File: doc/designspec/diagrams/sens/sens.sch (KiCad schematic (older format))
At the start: 16 parts

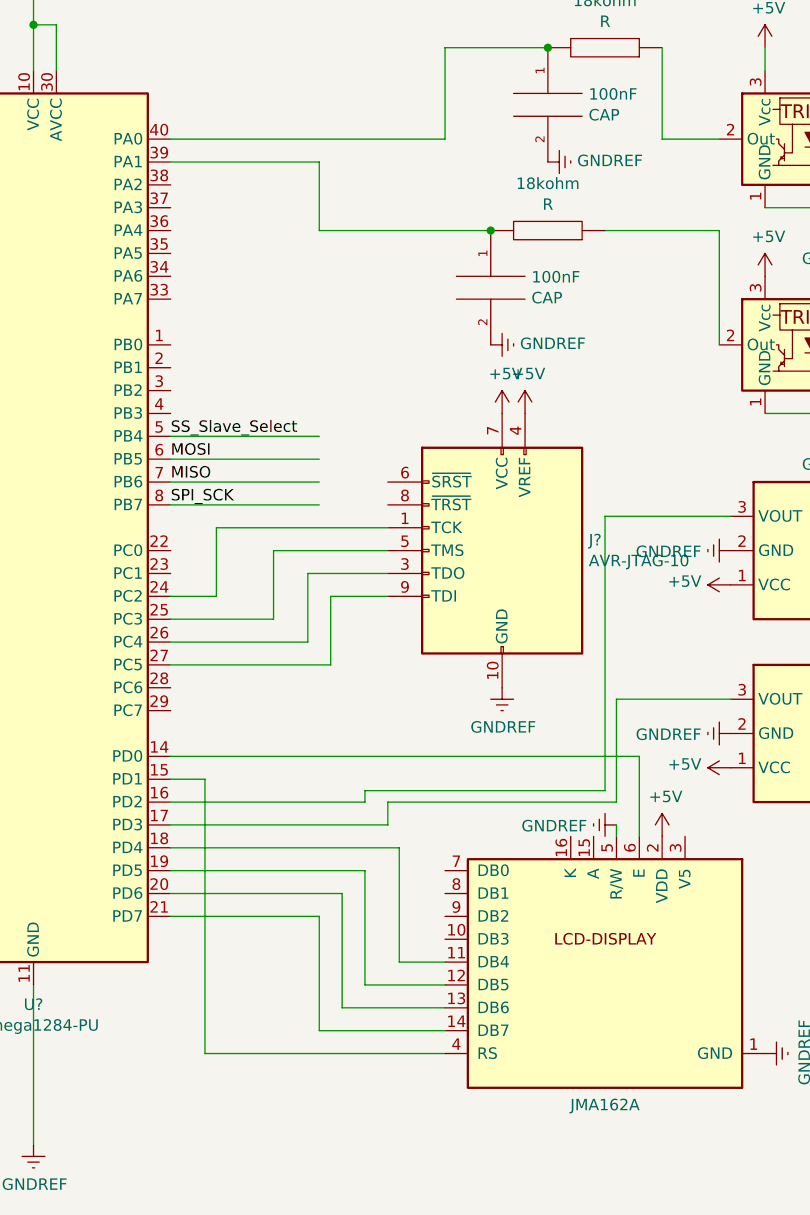
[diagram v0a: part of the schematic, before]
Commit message: update sens module schematic
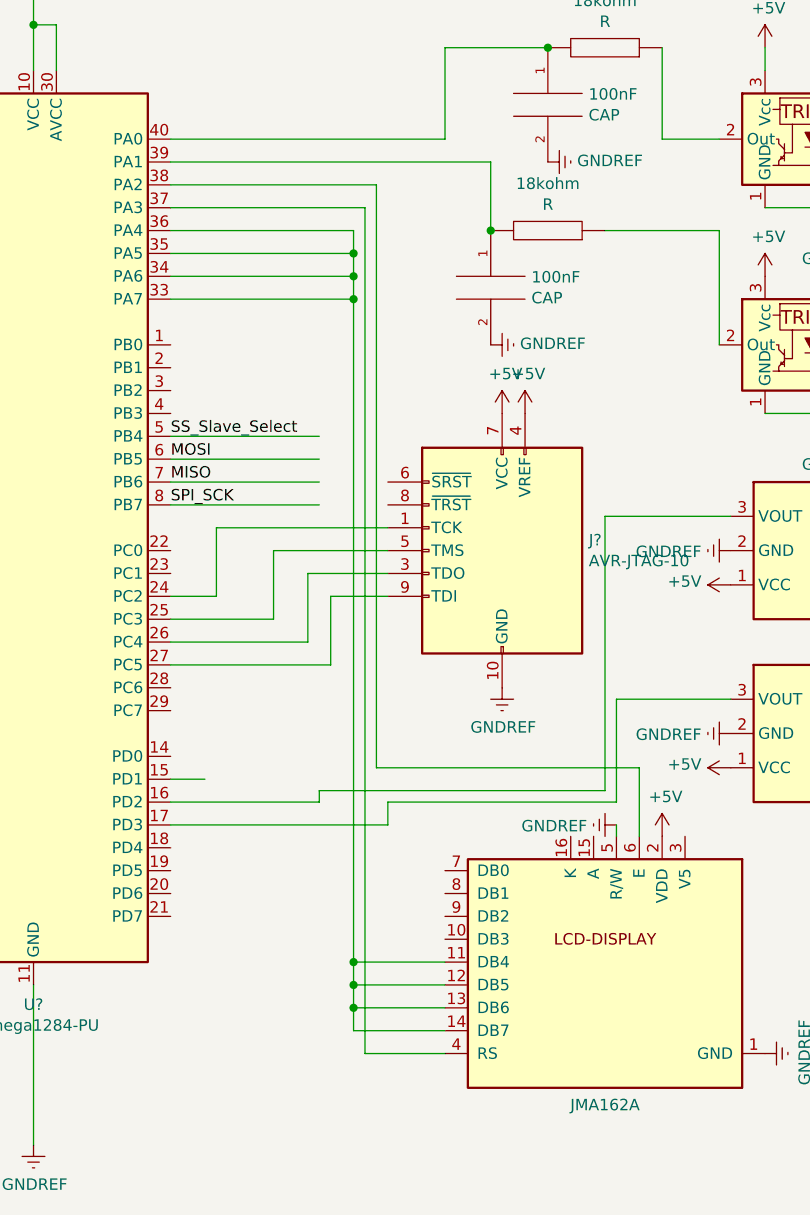
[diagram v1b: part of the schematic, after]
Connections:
- wire segments 74 -> 79

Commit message: Revert "update sens module schematic"
This reverts commit 18ae42b13ac670fb9527cdf2e035fc7bce516c1b.
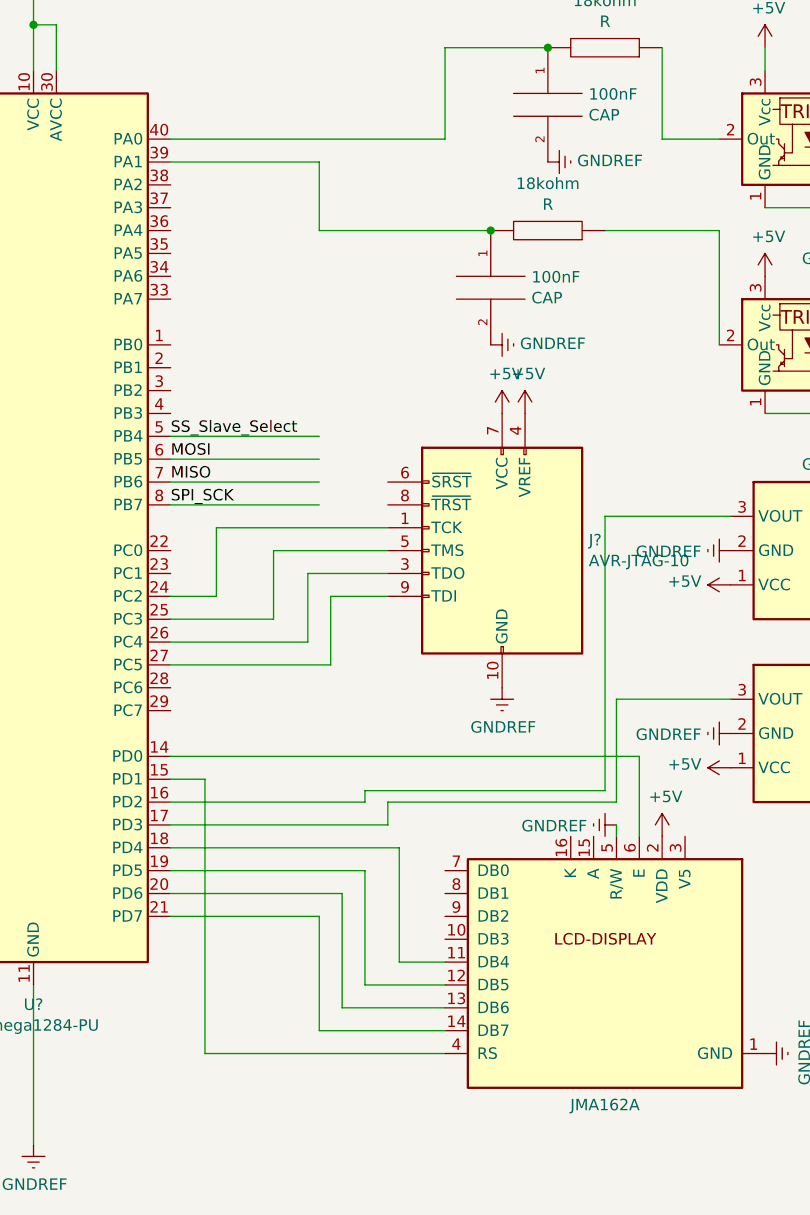
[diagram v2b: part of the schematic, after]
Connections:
- wire segments 79 -> 74
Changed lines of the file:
@@
 Wire Wire Line
 	3700 5150 3700 5850
+Wire Wire Line
+	6900 1050 6900 1150
 $Comp
 L sens-rescue:IQEXO-3-exo3 KRISTALLOSCILLATOR
@@
 	1    0    0    -1
 $EndComp
+$Comp
+L power:GNDREF #PWR?
+U 1 1 5BDF1A61
+P 6900 5450
+F 0 "#PWR?" H 6900 5200 50  0001 C CNN
+F 1 "GNDREF" H 6905 5277 50  0000 C CNN
+F 2 "" H 6900 5450 50  0001 C CNN
+F 3 "" H 6900 5450 50  0001 C CNN
+	1    6900 5450
+	0    -1   -1   0
+$EndComp
 Text Label 4300 2750 0    50   ~ 0
 SS_Slave_Select
@@
 $EndComp
 $Comp
+L sens-rescue:ACS715xLCTR-30A-taxi-sens-rescue AVSTÅNDSMÄTARE(FRAM)
+U 1 1 5BC4BC08
+P 7000 2350
+F 0 "AVSTÅNDSMÄTARE(FRAM)" H 6300 2450 50  0000 C CNN
+F 1 "GP2Y0A02YK" H 6350 2350 50  0000 C CNN
+F 2 "Package_SO:SOIC-8_3.9x4.9mm_P1.27mm" H 7100 2000 50  0001 L CIN
+F 3 "http://www.allegromicro.com/~/media/Files/Datasheets/ACS715-Datasheet.ashx?la=en" H 7000 2350 50  0001 C CNN
+	1    7000 2350
+	-1   0    0    -1
+$EndComp
+$Comp
 L power:+5V #PWR?
 U 1 1 5BE2925C
@@
 	1    0    0    -1
 $EndComp
+Wire Wire Line
+	6900 1750 7200 1750
+Wire Wire Line
+	7200 1750 7200 1800
 Wire Wire Line
 	6900 2650 7200 2650
@@
 $EndComp
 Wire Wire Line
+	6700 1450 6450 1450
+Wire Wire Line
+	6450 1450 6450 1050
+Wire Wire Line
 	6700 2350 6700 1850
 Wire Wire Line
 	6700 1850 6200 1850
+Wire Wire Line
+	5700 1850 4950 1850
+Connection ~ 5700 1850
 $Comp
 L power:GNDREF #PWR?
@@
 	0    -1   -1   0
 $EndComp
+Wire Wire Line
+	5950 1050 5500 1050
+Wire Wire Line
+	5500 1050 5500 1450
+Wire Wire Line
+	4300 1450 5500 1450
+Connection ~ 5950 1050
+Wire Wire Line
+	4300 1550 4950 1550
+Wire Wire Line
+	4950 1550 4950 1850
 $Comp
 L pspice:CAP C?
@@
 	3700 950  3700 1150
 $Comp
+L power:GNDREF #PWR?
+U 1 1 5BEC8E66
+P 6250 4450
+F 0 "#PWR?" H 6250 4200 50  0001 C CNN
+F 1 "GNDREF" V 6255 4322 50  0000 R CNN
+F 2 "" H 6250 4450 50  0001 C CNN
+F 3 "" H 6250 4450 50  0001 C CNN
+	1    6250 4450
+	0    1    1    0
+$EndComp
+Wire Wire Line
+	6250 4500 6250 4450
+$Comp
 L power:+5V #PWR?
 U 1 1 5BED369E
@@
 	6750 3900 6250 3900
 Wire Wire Line
+	5500 5050 5300 5050
+Wire Wire Line
+	5300 5050 5300 4550
+Wire Wire Line
+	5300 4550 4300 4550
+Wire Wire Line
 	4300 3450 4500 3450
 Wire Wire Line
@@
 	5000 3450 5250 3450
 Wire Wire Line
+	5500 5150 5150 5150
+Wire Wire Line
+	5150 5150 5150 4650
+Wire Wire Line
+	5150 4650 4300 4650
+Wire Wire Line
+	5500 5250 5050 5250
+Wire Wire Line
+	5050 5250 5050 4750
+Wire Wire Line
+	5050 4750 4300 4750
+Wire Wire Line
+	5500 5350 4950 5350
+Wire Wire Line
+	4950 5350 4950 4850
+Wire Wire Line
+	4950 4850 4300 4850
+Wire Wire Line
 	6250 3900 6250 4350
 Wire Wire Line
@@
 Wire Wire Line
 	6200 3100 6200 4300
+Wire Wire Line
+	6200 4300 5150 4300
+Wire Wire Line
+	5150 4300 5150 4350
+Wire Wire Line
+	5150 4350 4300 4350
+Wire Wire Line
+	5500 5450 4450 5450
+Wire Wire Line
+	4450 5450 4450 4250
+Wire Wire Line
+	4450 4250 4300 4250
+Wire Wire Line
+	6350 4150 4300 4150
+Wire Wire Line
+	6350 4150 6350 4500
 $Comp
 L power:GNDREF #PWR?
@@
 	1    0    0    -1
 $EndComp
-$Comp
-L sens-rescue:ACS715xLCTR-30A-taxi-sens-rescue AVSTÅNDSMÄTARE(FRAM)
-U 1 1 5BC4BC08
-P 7000 2350
-F 0 "AVSTÅNDSMÄTARE(FRAM)" H 6300 2450 50  0000 C CNN
-F 1 "GP2Y0A02YK" H 6350 2350 50  0000 C CNN
-F 2 "Package_SO:SOIC-8_3.9x4.9mm_P1.27mm" H 7100 2000 50  0001 L CIN
-F 3 "http://www.allegromicro.com/~/media/Files/Datasheets/ACS715-Datasheet.ashx?la=en" H 7000 2350 50  0001 C CNN
-	1    7000 2350
-	-1   0    0    -1
-$EndComp
-Wire Wire Line
-	5950 1050 5500 1050
-Wire Wire Line
-	4300 1450 5500 1450
-Wire Wire Line
-	5500 1050 5500 1450
-Connection ~ 5950 1050
-Wire Wire Line
-	6450 1450 6450 1050
-Wire Wire Line
-	6700 1450 6450 1450
-Wire Wire Line
-	6900 1050 6900 1150
-Wire Wire Line
-	7200 1750 7200 1800
-Wire Wire Line
-	6900 1750 7200 1750
-Wire Wire Line
-	6250 4500 6250 4450
-$Comp
-L power:GNDREF #PWR?
-U 1 1 5BEC8E66
-P 6250 4450
-F 0 "#PWR?" H 6250 4200 50  0001 C CNN
-F 1 "GNDREF" V 6255 4322 50  0000 R CNN
-F 2 "" H 6250 4450 50  0001 C CNN
-F 3 "" H 6250 4450 50  0001 C CNN
-	1    6250 4450
-	0    1    1    0
-$EndComp
-$Comp
-L power:GNDREF #PWR?
-U 1 1 5BDF1A61
-P 6900 5450
-F 0 "#PWR?" H 6900 5200 50  0001 C CNN
-F 1 "GNDREF" H 6905 5277 50  0000 C CNN
-F 2 "" H 6900 5450 50  0001 C CNN
-F 3 "" H 6900 5450 50  0001 C CNN
-	1    6900 5450
-	0    -1   -1   0
-$EndComp
-Wire Wire Line
-	4450 4250 4300 4250
-Wire Wire Line
-	6350 4500 6350 4200
-Wire Wire Line
-	6350 4200 5200 4200
-Wire Wire Line
-	5200 4200 5200 1650
-Wire Wire Line
-	5200 1650 4300 1650
-Wire Wire Line
-	5500 5350 5100 5350
-Connection ~ 5700 1850
-Wire Wire Line
-	5700 1850 5700 1550
-Wire Wire Line
-	4300 1550 5700 1550
-Wire Wire Line
-	5100 1850 4300 1850
-Wire Wire Line
-	5100 1850 5100 1950
-Wire Wire Line
-	5100 1950 4300 1950
-Connection ~ 5100 1950
-Wire Wire Line
-	5100 1950 5100 2050
-Wire Wire Line
-	5100 2050 4300 2050
-Connection ~ 5100 2050
-Wire Wire Line
-	5100 2050 5100 2150
-Wire Wire Line
-	5100 2150 4300 2150
-Connection ~ 5100 2150
-Wire Wire Line
-	5100 2150 5100 5050
-Wire Wire Line
-	5500 5250 5100 5250
-Connection ~ 5100 5250
-Wire Wire Line
-	5100 5250 5100 5350
-Wire Wire Line
-	5500 5150 5100 5150
-Connection ~ 5100 5150
-Wire Wire Line
-	5100 5150 5100 5250
-Wire Wire Line
-	5500 5050 5100 5050
-Connection ~ 5100 5050
-Wire Wire Line
-	5100 5050 5100 5150
-Wire Wire Line
-	5500 5450 5150 5450
-Wire Wire Line
-	5150 1750 4300 1750
-Wire Wire Line
-	6200 4300 4950 4300
-Wire Wire Line
-	4950 4300 4950 4350
-Wire Wire Line
-	4950 4350 4300 4350
-Wire Wire Line
-	5150 1750 5150 5450
 $EndSCHEMATC
